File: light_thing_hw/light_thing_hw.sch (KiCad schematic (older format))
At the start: 62 parts, among them J1 CONNECTORS, J2 Li-Ion Battery, J3 ADDR_LED_PANEL_1_CONNECTORS, J4 ADDR_LED_PANEL_2_CONNECTORS, J5 MIC_CONN, J6 3V3_TP, Q1 MMBF170, Q2 BSS83P, SW1 ST_USER_BUTTON1, SW2 ST_RESET_BUTTON, U1 BC832-V1, U2 BQ21040DBVT, U4 LMR62421XMF, U5 LP38511MRX-ADJ_NOPB, U6 STM32L476RGTx, U7 ICM-20600

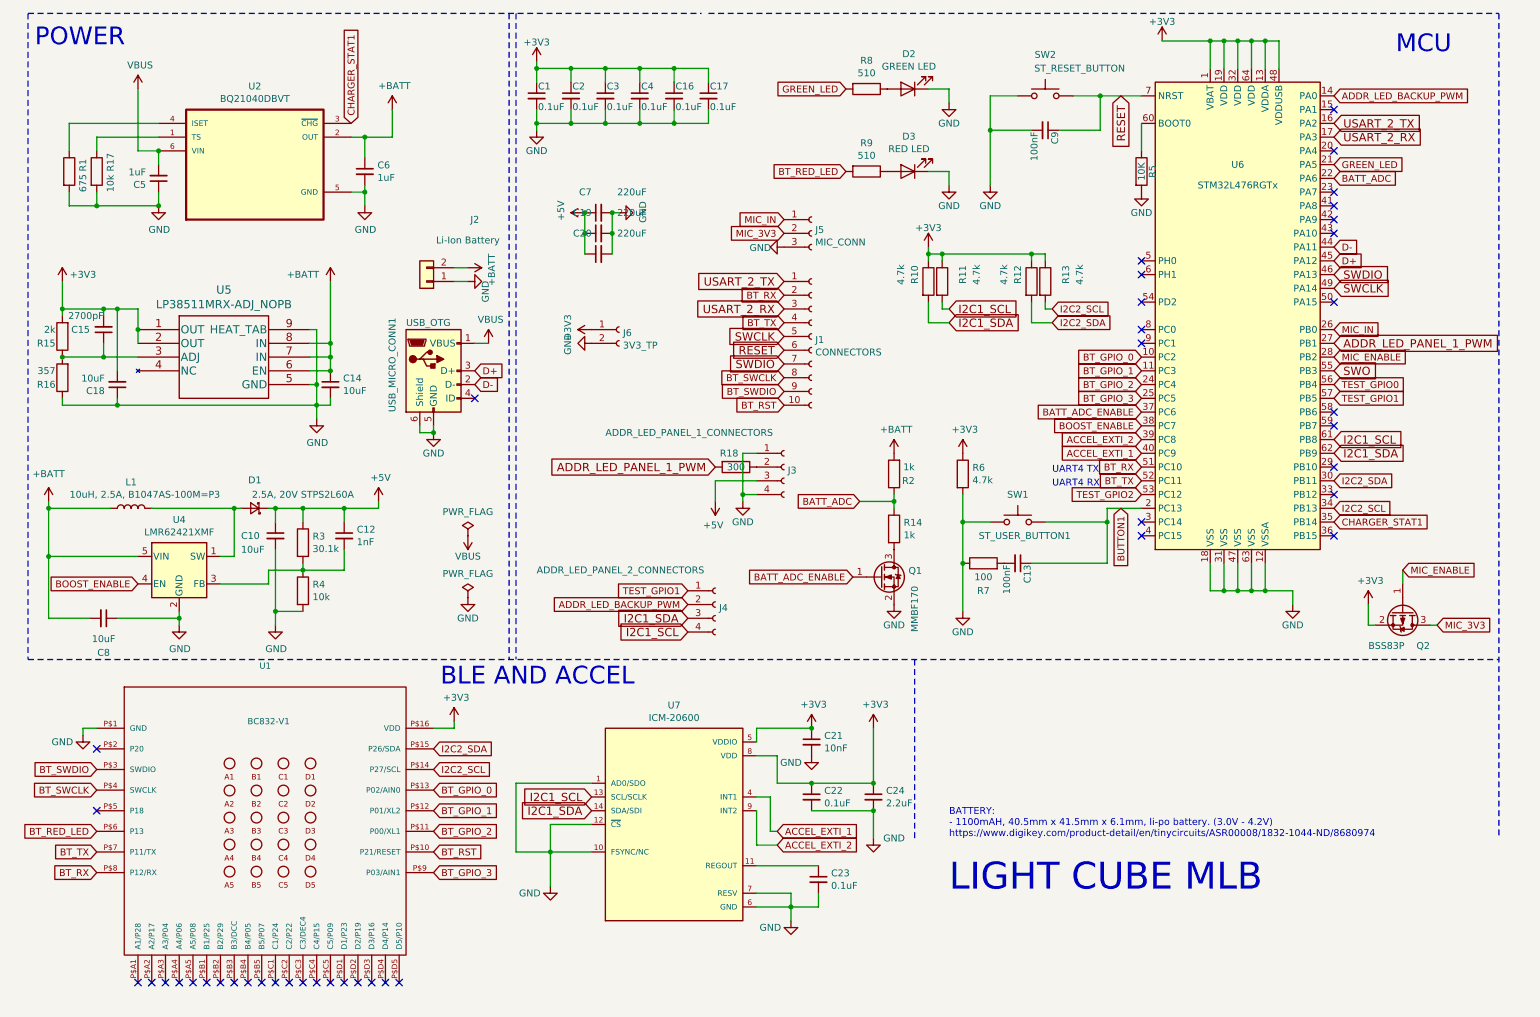
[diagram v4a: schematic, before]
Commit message: changed userbutton and connector footprints
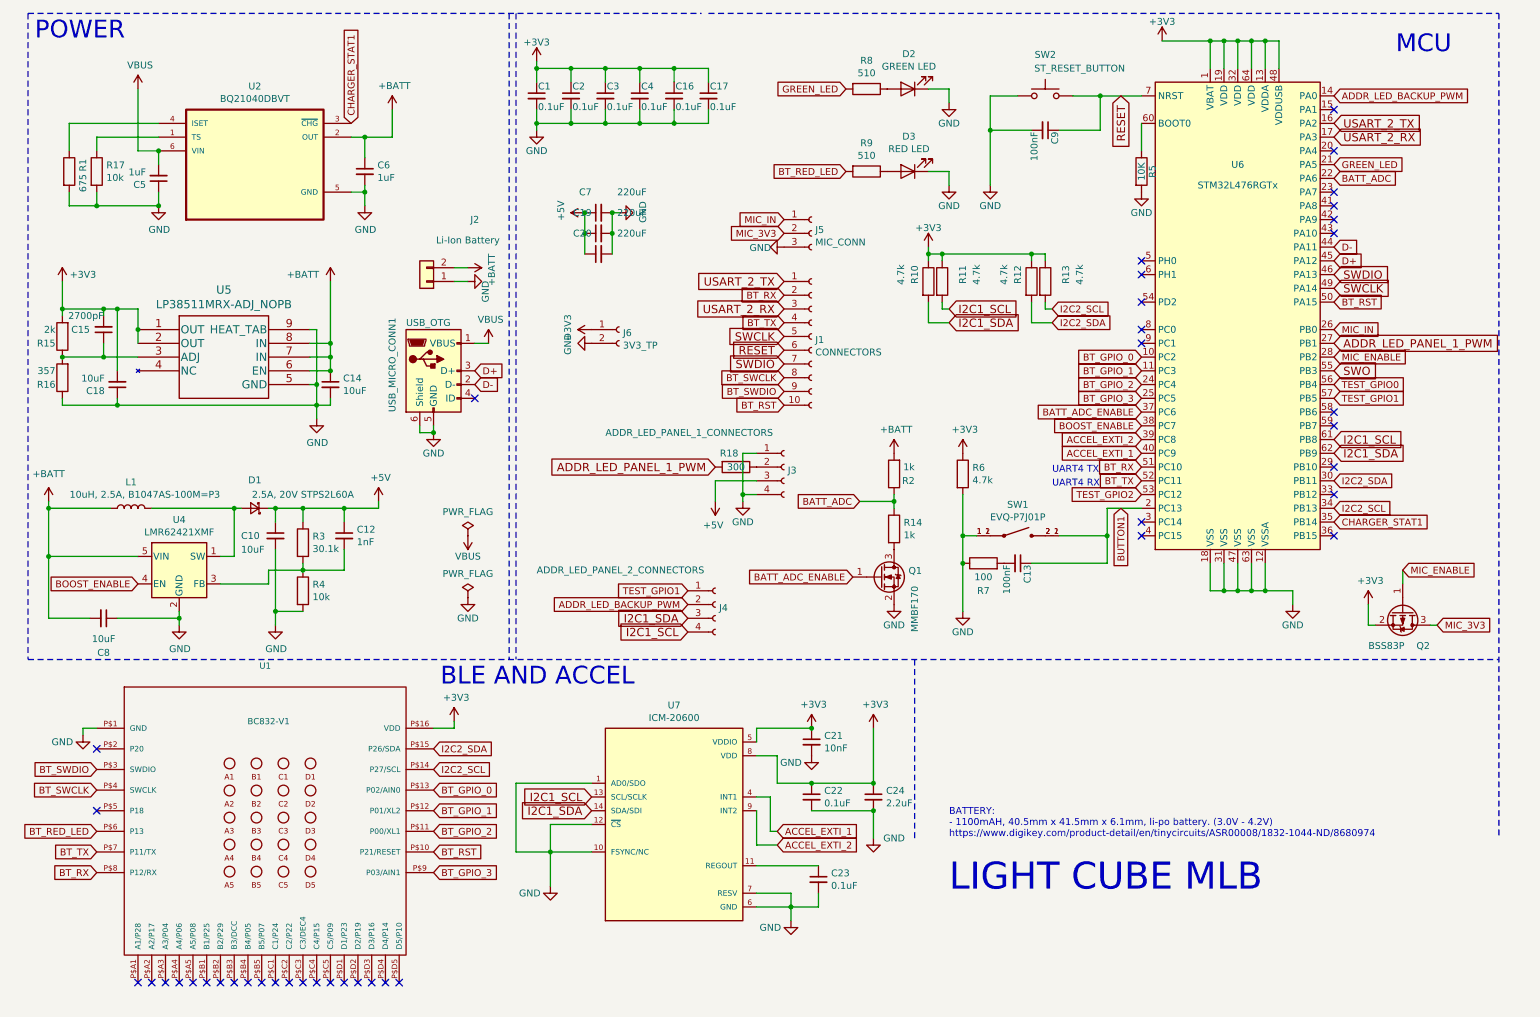
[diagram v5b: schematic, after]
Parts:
- removed SW1: ST_USER_BUTTON1, Button_Switch_SMD:SW_SPST_B3U-3000P, symbol Switch:SW_Push
- added SW1: EVQ-P7J01P, EVQ-P7J01P_smt_right_angle_tactile_switch:SW_EVQ-P7J01P, symbol EVQ-P7J01P_smt_right_angle_tactile_switch:EVQ-P7J01P
- J1: footprint Connector_PinHeader_1.00mm:PinHeader_2x05_P1.00mm_Vertical -> Connector_PinHeader_2.54mm:PinHeader_2x05_P2.54mm_Vertical
- J6: footprint Connector_PinHeader_1.00mm:PinHeader_2x01_P1.00mm_Vertical -> Connector_PinHeader_2.54mm:PinHeader_2x01_P2.54mm_Vertical
- R17: JLC_LIBRARY C21190 -> C25804
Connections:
- net BT_RST: now also U6.50 (PA15)
- net BUTTON1: now also SW1.2_1, SW1.2_2
- net GND: now also SW1.1_1, SW1.1_2
- no-connect marks 42 -> 41
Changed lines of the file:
@@
 $EndComp
-Wire Wire Line
-	7500 4200 7300 4200
 Wire Wire Line
 	8600 4100 8350 4100
@@
 	0    -1   -1   0
 $EndComp
-Wire Wire Line
-	7300 4200 7300 4500
 Connection ~ 7300 4500
 Wire Wire Line
 	7300 4500 7300 4850
-Wire Wire Line
-	7300 4200 7300 4000
-Connection ~ 7300 4200
 $Comp
 L Device:R R6
@@
 Wire Notes Line
 	500  500  5400 500
-Text Notes 550  750  0    129  ~ 0
+Text Notes 550  700  0    129  ~ 0
 POWER
 Wire Notes Line
@@
 BLE AND ACCEL
 Wire Wire Line
-	7900 4200 8350 4200
-Wire Wire Line
 	7800 4500 8350 4500
 Text GLabel 6000 2450 0    60   Input ~ 0
@@
 F 3 "" H 7900 1300 50  0001 C CNN
 	1    7900 1100
-	1    0    0    -1
-$EndComp
-$Comp
-L Switch:SW_Push SW1
-U 1 1 5F1F7389
-P 7700 4200
-F 0 "SW1" H 7700 4400 50  0000 C CNN
-F 1 "ST_USER_BUTTON1" H 7750 4100 50  0000 C CNN
-F 2 "Button_Switch_SMD:SW_SPST_B3U-3000P" H 7700 4400 50  0001 C CNN
-F 3 "" H 7700 4400 50  0001 C CNN
-	1    7700 4200
 	1    0    0    -1
 $EndComp
@@
 F 0 "J1" H 6227 2826 50  0000 L CNN
 F 1 "CONNECTORS" H 6227 2735 50  0000 L CNN
-F 2 "Connector_PinHeader_1.00mm:PinHeader_2x05_P1.00mm_Vertical" H 6200 2850 50  0001 C CNN
+F 2 "Connector_PinHeader_2.54mm:PinHeader_2x05_P2.54mm_Vertical" H 6200 2850 50  0001 C CNN
 F 3 "~" H 6200 2850 50  0001 C CNN
 	1    6200 2850
@@
 Connection ~ 4750 1950
 $Comp
-L MCU_ST_STM32L4:STM32L476RGTx U6
-U 1 1 5F38D810
-P 9300 2700
-F 0 "U6" H 9300 3800 50  0000 C CNN
-F 1 "STM32L476RGTx" H 9300 3650 50  0000 C CNN
-F 2 "Package_QFP:LQFP-64_10x10mm_P0.5mm" H 8700 1000 50  0001 R CNN
-F 3 "http://www.st.com/st-web-ui/static/active/en/resource/technical/document/datasheet/DM00108832.pdf" H 9300 2700 50  0001 C CNN
-F 4 "C74797" H 9300 2700 50  0001 C CNN "JLC_LIBRARY"
-	1    9300 2700
-	1    0    0    -1
-$EndComp
-$Comp
 L power:+3V3 #PWR0116
 U 1 1 5F39CA0A
@@
 	1    0    0    -1
 $EndComp
-Wire Wire Line
-	9600 900  9600 700
 Connection ~ 9100 700
-Wire Wire Line
-	9100 900  9100 700
 Wire Wire Line
 	9600 700  9500 700
 Connection ~ 9500 700
 Wire Wire Line
-	9500 700  9500 900
-Wire Wire Line
 	9400 700  9500 700
 Connection ~ 9400 700
 Wire Wire Line
-	9400 700  9400 900
-Wire Wire Line
 	9300 700  9400 700
 Connection ~ 9300 700
 Wire Wire Line
-	9300 700  9300 900
-Wire Wire Line
 	9100 700  9200 700
 Wire Wire Line
 	9200 700  9300 700
 Connection ~ 9200 700
-Wire Wire Line
-	9200 900  9200 700
 Text GLabel 10000 1600 2    50   Input ~ 0
 GREEN_LED
@@
 Text GLabel 8600 3300 0    50   Input ~ 0
 BT_GPIO_3
-Text GLabel 10000 2800 2    50   Input ~ 0
-MIC_IN
 Text GLabel 10000 1700 2    50   Input ~ 0
 BATT_ADC
@@
 NoConn ~ 10000 2000
 NoConn ~ 10000 2100
-NoConn ~ 10000 2600
 NoConn ~ 10000 3800
 NoConn ~ 10000 4000
@@
 F 0 "J6" H 4828 2776 50  0000 L CNN
 F 1 "3V3_TP" H 4828 2685 50  0000 L CNN
-F 2 "Connector_PinHeader_1.00mm:PinHeader_2x01_P1.00mm_Vertical" H 4800 2800 50  0001 C CNN
+F 2 "Connector_PinHeader_2.54mm:PinHeader_2x01_P2.54mm_Vertical" H 4800 2800 50  0001 C CNN
 F 3 "~" H 4800 2800 50  0001 C CNN
 	1    4800 2800
 	1    0    0    -1
 $EndComp
-Connection ~ 8350 4200
-Wire Wire Line
-	8350 4100 8350 4200
-Wire Wire Line
-	8350 4200 8350 4500
 Text GLabel 5300 4900 0    60   Input ~ 0
 I2C1_SDA
@@
 Connection ~ 2950 1400
 $Comp
-L Device:R R17
-U 1 1 601ECAC0
-P 1000 1650
-F 0 "R17" V 1100 1650 50  0000 L CNN
-F 1 "10k" V 1100 1500 50  0000 L CNN
-F 2 "Resistor_SMD:R_0603_1608Metric_Pad1.05x0.95mm_HandSolder" V 930 1650 50  0001 C CNN
-F 3 "~" H 1000 1650 50  0001 C CNN
-F 4 "C21190" H 1000 1650 50  0001 C CNN "JLC_LIBRARY"
-	1    1000 1650
-	1    0    0    -1
-$EndComp
-$Comp
 L power:GND #PWR0107
 U 1 1 602388CD
@@
 $EndComp
 NoConn ~ 10000 4300
+$Comp
+L EVQ-P7J01P_smt_right_angle_tactile_switch:EVQ-P7J01P SW1
+U 1 1 60412875
+P 7700 4300
+F 0 "SW1" H 7700 4527 50  0000 C CNN
+F 1 "EVQ-P7J01P" H 7700 4436 50  0000 C CNN
+F 2 "EVQ-P7J01P_smt_right_angle_tactile_switch:SW_EVQ-P7J01P" H 7700 4300 50  0001 L BNN
+F 3 "" H 7700 4300 50  0001 L BNN
+F 4 "Manufacturer Recommendation" H 7700 4300 50  0001 L BNN "STANDARD"
+F 5 "Panasonic" H 7700 4300 50  0001 L BNN "MANUFACTURER"
+	1    7700 4300
+	1    0    0    -1
+$EndComp
+Wire Wire Line
+	7300 4000 7300 4300
+Wire Wire Line
+	8350 4100 8350 4300
+Wire Wire Line
+	7400 4300 7300 4300
+Connection ~ 7300 4300
+Wire Wire Line
+	7300 4300 7300 4500
+Wire Wire Line
+	8000 4300 8350 4300
+Connection ~ 8350 4300
+Wire Wire Line
+	8350 4300 8350 4500
+Wire Wire Line
+	9600 900  9600 700
+Wire Wire Line
+	9500 700  9500 900
+Wire Wire Line
+	9400 700  9400 900
+Wire Wire Line
+	9300 700  9300 900
+Wire Wire Line
+	9200 900  9200 700
+Wire Wire Line
+	9100 900  9100 700
+$Comp
+L MCU_ST_STM32L4:STM32L476RGTx U6
+U 1 1 5F38D810
+P 9300 2700
+F 0 "U6" H 9300 3800 50  0000 C CNN
+F 1 "STM32L476RGTx" H 9300 3650 50  0000 C CNN
+F 2 "Package_QFP:LQFP-64_10x10mm_P0.5mm" H 8700 1000 50  0001 R CNN
+F 3 "http://www.st.com/st-web-ui/static/active/en/resource/technical/document/datasheet/DM00108832.pdf" H 9300 2700 50  0001 C CNN
+F 4 "C74797" H 9300 2700 50  0001 C CNN "JLC_LIBRARY"
+	1    9300 2700
+	1    0    0    -1
+$EndComp
+Text GLabel 10000 2600 2    50   Input ~ 0
+BT_RST
+Text GLabel 10000 2800 2    50   Input ~ 0
+MIC_IN
+$Comp
+L Device:R R17
+U 1 1 601AFD47
+P 1000 1650
+F 0 "R17" H 1070 1696 50  0000 L CNN
+F 1 "10k" H 1070 1605 50  0000 L CNN
+F 2 "Resistor_SMD:R_0603_1608Metric_Pad1.05x0.95mm_HandSolder" V 930 1650 50  0001 C CNN
+F 3 "~" H 1000 1650 50  0001 C CNN
+F 4 "C25804" H 1000 1650 50  0001 C CNN "JLC_LIBRARY"
+	1    1000 1650
+	1    0    0    -1
+$EndComp
 $EndSCHEMATC

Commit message: updates
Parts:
- C1, C13, C16, C17, C2, C3, C4, C9: symbol light_thing_hw-rescue:C_Small -> light_thing_hw-rescue:C_Small-light_thing_hw-rescue
- R5: symbol light_thing_hw-rescue:R -> light_thing_hw-rescue:R-light_thing_hw-rescue
- U2: JLC_LIBRARY (none) -> C78978
- U7: JLC_LIBRARY (none) -> C124140
- USB_MICRO_CONN1: symbol light_thing_hw-rescue:USB_OTG -> light_thing_hw-rescue:USB_OTG-light_thing_hw-rescue
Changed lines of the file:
@@
 $EndComp
 $Comp
-L light_thing_hw-rescue:C_Small C9
+L light_thing_hw-rescue:C_Small-light_thing_hw-rescue C9
 U 1 1 5EBF990E
 P 7900 1350
@@
 Connection ~ 7500 1350
 $Comp
-L light_thing_hw-rescue:R R5
+L light_thing_hw-rescue:R-light_thing_hw-rescue R5
 U 1 1 5EBFB07E
 P 8600 1650
@@
 $EndComp
 $Comp
-L light_thing_hw-rescue:USB_OTG USB_MICRO_CONN1
+L light_thing_hw-rescue:USB_OTG-light_thing_hw-rescue USB_MICRO_CONN1
 U 1 1 5EBFE33E
 P 3450 3100
@@
 BUTTON1
 $Comp
-L light_thing_hw-rescue:C_Small C13
+L light_thing_hw-rescue:C_Small-light_thing_hw-rescue C13
 U 1 1 5EEA19F9
 P 7700 4500
@@
 	2300 4100 2500 4100
 $Comp
-L light_thing_hw-rescue:C_Small C1
+L light_thing_hw-rescue:C_Small-light_thing_hw-rescue C1
 U 1 1 5EE590BE
 P 4200 1100
@@
 $EndComp
 $Comp
-L light_thing_hw-rescue:C_Small C2
+L light_thing_hw-rescue:C_Small-light_thing_hw-rescue C2
 U 1 1 5EE73B85
 P 4450 1100
@@
 $EndComp
 $Comp
-L light_thing_hw-rescue:C_Small C3
+L light_thing_hw-rescue:C_Small-light_thing_hw-rescue C3
 U 1 1 5EE7C964
 P 4700 1100
@@
 $EndComp
 $Comp
-L light_thing_hw-rescue:C_Small C4
+L light_thing_hw-rescue:C_Small-light_thing_hw-rescue C4
 U 1 1 5EE8573C
 P 4950 1100
@@
 $EndComp
 $Comp
-L light_thing_hw-rescue:C_Small C16
+L light_thing_hw-rescue:C_Small-light_thing_hw-rescue C16
 U 1 1 5EE8E535
 P 5200 1100
@@
 $EndComp
 $Comp
-L light_thing_hw-rescue:C_Small C17
+L light_thing_hw-rescue:C_Small-light_thing_hw-rescue C17
 U 1 1 5EE8E53B
 P 5450 1100
@@
 F 9 "Low-Power, High-Performance Integrated 6-Axis MEMS MotionTracking Device in 2.5mm x 3mm Package" H 5200 6400 50  0001 L BNN "DESCRIPTION"
 F 10 "TDK InvenSense" H 5200 6400 50  0001 L BNN "MF"
+F 11 "C124140" H 5200 6400 50  0001 C CNN "JLC_LIBRARY"
 	1    5200 6400
 	1    0    0    -1
@@
 F 2 "TI_BQ21040DBVT:SOT95P280X145-6N" H 2150 1600 50  0001 L BNN
 F 3 "" H 2150 1600 50  0001 L BNN
+F 4 "C78978" H 2150 1600 50  0001 C CNN "JLC_LIBRARY"
 	1    2150 1600
 	1    0    0    -1
